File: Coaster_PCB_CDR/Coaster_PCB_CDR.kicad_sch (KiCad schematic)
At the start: 34 parts, among them J1 Vin, J10 GPIO_0-1, J11 5v, J12 5v, J13 GPIO_14-15, J14 5v, J15 GPIO_27-28, J16 5v, J17 5v, J2 Vin, J3 HC-05, J4 HC-05, J5 VCC_Batt, J6 3v3, J7 10V, J8 qwiic, J9 3v3, SW1 Vin_Switch, SW2 Vin_Switch, SW3 Vin_Switch, U1 PicoW, U2 LM2937xT

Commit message: final please
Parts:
- removed H2: M, MountingHole:MountingHole_4.3mm_M4_Pad_Via, symbol Mechanical:MountingHole_Pad
- added J10: qwiic, Connector_JST:JST_SH_SM04B-SRSS-TB_1x04-1MP_P1.00mm_Horizontal, symbol Connector_Generic:Conn_01x04
- renumbered H3 to H2, J10 to J12, J12 to J13, J13 to J15, J15 to J17, J17 to J18, J5 to J3, J3 to J4, J7 to J5, J4 to J6, J6 to J7, J9 to J8, J8 to J9
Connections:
- net +3V3: now also J10.2 (Pin_2)
- net GND: now also J10.1 (Pin_1)
- net GPIO0: now also J10.3 (Pin_3)
- net GPIO1: now also J10.4 (Pin_4)
- no-connect marks 13 -> 12
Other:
- moved on the sheet: C1, C2, D1, D2, H2, R1, SW1

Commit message: final finalish
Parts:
- added C1: 2200uF, Capacitor_THT:CP_Radial_D10.0mm_P5.00mm, symbol M5_BuggyProject-rescue:CP-Device
- SW1: value Vin_Switch -> sigma
- SW2: renamed from SW3; value Vin_Switch -> alpha
- SW3: renamed from SW2; value Vin_Switch -> beta
- renumbered C1 to C2, C2 to C3, J11 to J10, J12 to J11, J13 to J12, J14 to J13, J15 to J14, J16 to J15, J17 to J16, J10 to J17
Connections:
- net GND: now also C1.2
- net VCC_Batt: now also C1.1
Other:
- moved on the sheet: SW3

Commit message: some refinements
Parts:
- added J12: 5v, Connector_PinSocket_2.54mm:PinSocket_1x02_P2.54mm_Vertical, symbol Connector_Generic:Conn_01x02
- renumbered J12 to J13, J13 to J14, J14 to J15, J15 to J16, J16 to J17, J17 to J18, J18 to J19
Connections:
- net +5V: now also J12.2 (Pin_2)
- net GND: now also J12.1 (Pin_1)

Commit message: antooonie
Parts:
- removed J3: VCC_Batt, TestPoint:TestPoint_Plated_Hole_D5.0mm, symbol Connector_Generic:Conn_01x01
- J5: footprint TestPoint:TestPoint_Plated_Hole_D5.0mm -> TestPoint:TestPoint_Plated_Hole_D3.0mm
- R1: value 330 -> 1k; footprint Resistor_THT:R_Axial_DIN0204_L3.6mm_D1.6mm_P7.62mm_Horizontal -> Resistor_THT:R_Axial_DIN0207_L6.3mm_D2.5mm_P10.16mm_Horizontal
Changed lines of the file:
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@@
-    )
-  )
-  (global_label "VCC_Batt" (shape input) (at 101.6 130.81 90) (fields_autoplaced)
-    (effects (font (size 1.27 1.27)) (justify left))
-    (property "Intersheet References" "${INTERSHEET_REFS}" (id 0) (at 101.5206 119.9302 90)
-      (effects (font (size 1.27 1.27)) (justify left) hide)
     )
   )
@@
     (in_bom yes) (on_board yes)
     (property "Reference" "R1" (id 0) (at 97.79 35.7886 90))
-    (property "Value" "330" (id 1) (at 97.79 38.1 90)
+    (property "Value" "1k" (id 1) (at 97.79 38.1 90)
       (effects (font (size 1.016 1.016)))
     )
-    (property "Footprint" "Resistor_THT:R_Axial_DIN0204_L3.6mm_D1.6mm_P7.62mm_Horizontal" (id 2) (at 97.79 38.862 90)
+    (property "Footprint" "Resistor_THT:R_Axial_DIN0207_L6.3mm_D2.5mm_P10.16mm_Horizontal" (id 2) (at 97.79 38.862 90)
       (effects (font (size 1.27 1.27)) hide)
     )
@@
       (effects (font (size 1.27 1.27)) (justify left))
     )
-    (property "Footprint" "TestPoint:TestPoint_Plated_Hole_D5.0mm" (id 2) (at 109.22 135.89 0)
+    (property "Footprint" "TestPoint:TestPoint_Plated_Hole_D3.0mm" (id 2) (at 109.22 135.89 0)
       (effects (font (size 1.27 1.27)) hide)
     )
@@
     )
     (property "Datasheet" "" (id 3) (at 160.02 129.54 0)
-      (effects (font (size 1.27 1.27)) hide)
-    )
-    (pin "1")
-  )
-  (symbol (lib_id "Connector_Generic:Conn_01x01") (at 101.6 135.89 270) (unit 1)
-    (in_bom yes) (on_board yes)
-    (property "Reference" "J3" (id 0) (at 103.632 132.6388 90)
-      (effects (font (size 1.27 1.27)) (justify left))
-    )
-    (property "Value" "VCC_Batt" (id 1) (at 97.79 138.43 90)
-      (effects (font (size 1.27 1.27)) (justify left))
-    )
-    (property "Footprint" "TestPoint:TestPoint_Plated_Hole_D5.0mm" (id 2) (at 101.6 135.89 0)
-      (effects (font (size 1.27 1.27)) hide)
-    )
-    (property "Datasheet" "~" (id 3) (at 101.6 135.89 0)
       (effects (font (size 1.27 1.27)) hide)
     )
@@
       (reference "J2") (unit 1) (value "Vin") (footprint "Connector_PinSocket_2.54mm:PinSocket_1x02_P2.54mm_Vertical")
     )
-    (path "/406bc657-f0d9-4cdc-a558-cd9bffd22dd4"
-      (reference "J3") (unit 1) (value "VCC_Batt") (footprint "TestPoint:TestPoint_Plated_Hole_D5.0mm")
-    )
     (path "/ac0cdac4-5ad6-4885-bc81-46c93e1ce041"
       (reference "J4") (unit 1) (value "HC-05") (footprint "Connector_PinSocket_2.54mm:PinSocket_1x06_P2.54mm_Vertical")
     )
     (path "/00000000-0000-0000-0000-0000627eac87"
-      (reference "J5") (unit 1) (value "10V") (footprint "TestPoint:TestPoint_Plated_Hole_D5.0mm")
+      (reference "J5") (unit 1) (value "10V") (footprint "TestPoint:TestPoint_Plated_Hole_D3.0mm")
     )
     (path "/7bcc4302-a9ff-46a0-92cd-33fd1db4d7ac"
@@
     )
     (path "/00000000-0000-0000-0000-000061de06ec"
-      (reference "R1") (unit 1) (value "330") (footprint "Resistor_THT:R_Axial_DIN0204_L3.6mm_D1.6mm_P7.62mm_Horizontal")
+      (reference "R1") (unit 1) (value "1k") (footprint "Resistor_THT:R_Axial_DIN0207_L6.3mm_D2.5mm_P10.16mm_Horizontal")
     )
     (path "/00000000-0000-0000-0000-000061d314d6"

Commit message: done with fdr pcb?
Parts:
- removed C1: 2200uF, Capacitor_THT:CP_Radial_D10.0mm_P5.00mm, symbol M5_BuggyProject-rescue:CP-Device
- removed J10, J12, J14, J16, J19: 5v, Connector_PinSocket_2.54mm:PinSocket_1x02_P2.54mm_Vertical, symbol Connector_Generic:Conn_01x02
- removed J2: Vin, Connector_PinSocket_2.54mm:PinSocket_1x02_P2.54mm_Vertical, symbol Connector_Generic:Conn_01x02
- removed J6: HC-05, Connector_PinSocket_2.54mm:PinSocket_1x06_P2.54mm_Vertical, symbol Connector_Generic:Conn_01x06
- removed J7: 3v3, Connector_PinSocket_2.54mm:PinSocket_1x02_P2.54mm_Vertical, symbol Connector_Generic:Conn_01x02
- removed SW2: alpha, Buggy_Footprints:omar_3pin_switch, symbol Switch:SW_SPDT
- removed SW3: beta, Buggy_Footprints:omar_3pin_switch, symbol Switch:SW_SPDT
- added SW1: sigma, Buggy_Footprints:omar_3pin_switch, symbol Switch:SW_SPDT
- renumbered C2 to C1, C3 to C2, J18 to J10, J4 to J2, J5 to J3, J8 to J4, J9 to J5, J11 to J6, J13 to J7, J15 to J8, J17 to J9, SW1 to SW2
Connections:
- net GPIO0: now also J2.5 (Pin_5); no longer J10.3 (Pin_3), J5.3 (Pin_3)
- net GPIO1: now also J2.4 (Pin_4); no longer J10.4 (Pin_4), J5.4 (Pin_4)
- net VCC: now also SW1.1 (A), SW1.2 (B), SW1.3 (C)
- net GPIO16: no longer names the net of U1.21 (GPIO16)
- net GPIO16: no longer J2.4 (Pin_4)
- net GPIO17: no longer names the net of U1.22 (GPIO17)
- net GPIO17: no longer J2.5 (Pin_5)
- net GPIO4 renamed SDA
- net SDA: now also J10.3 (Pin_3), J5.3 (Pin_3)
- net GPIO5 renamed SCL
- net SCL: now also J10.4 (Pin_4), J5.4 (Pin_4)

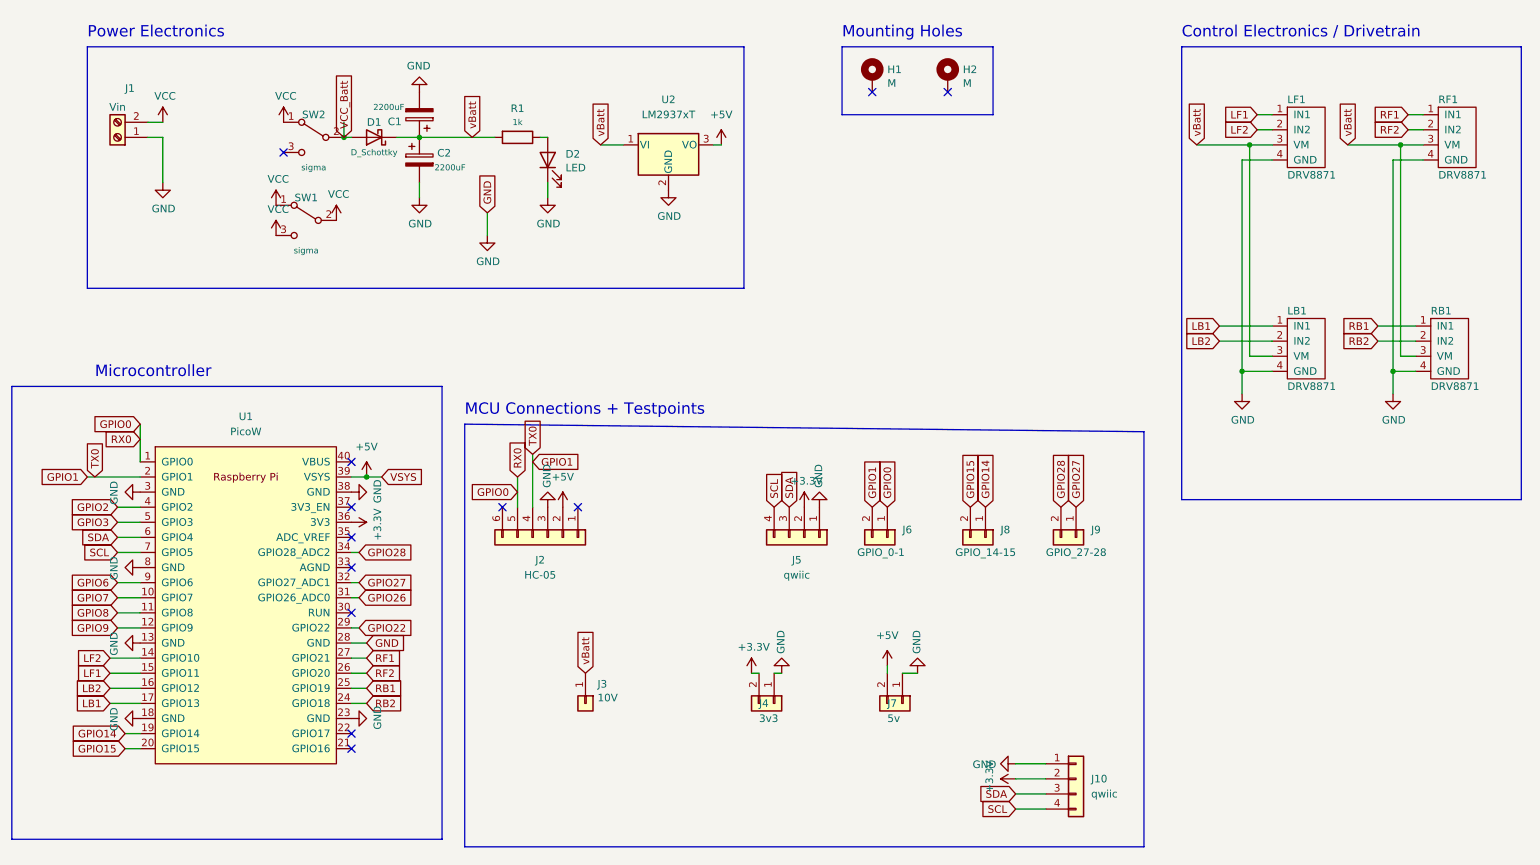
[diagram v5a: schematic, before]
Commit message: fdr pcb minimized
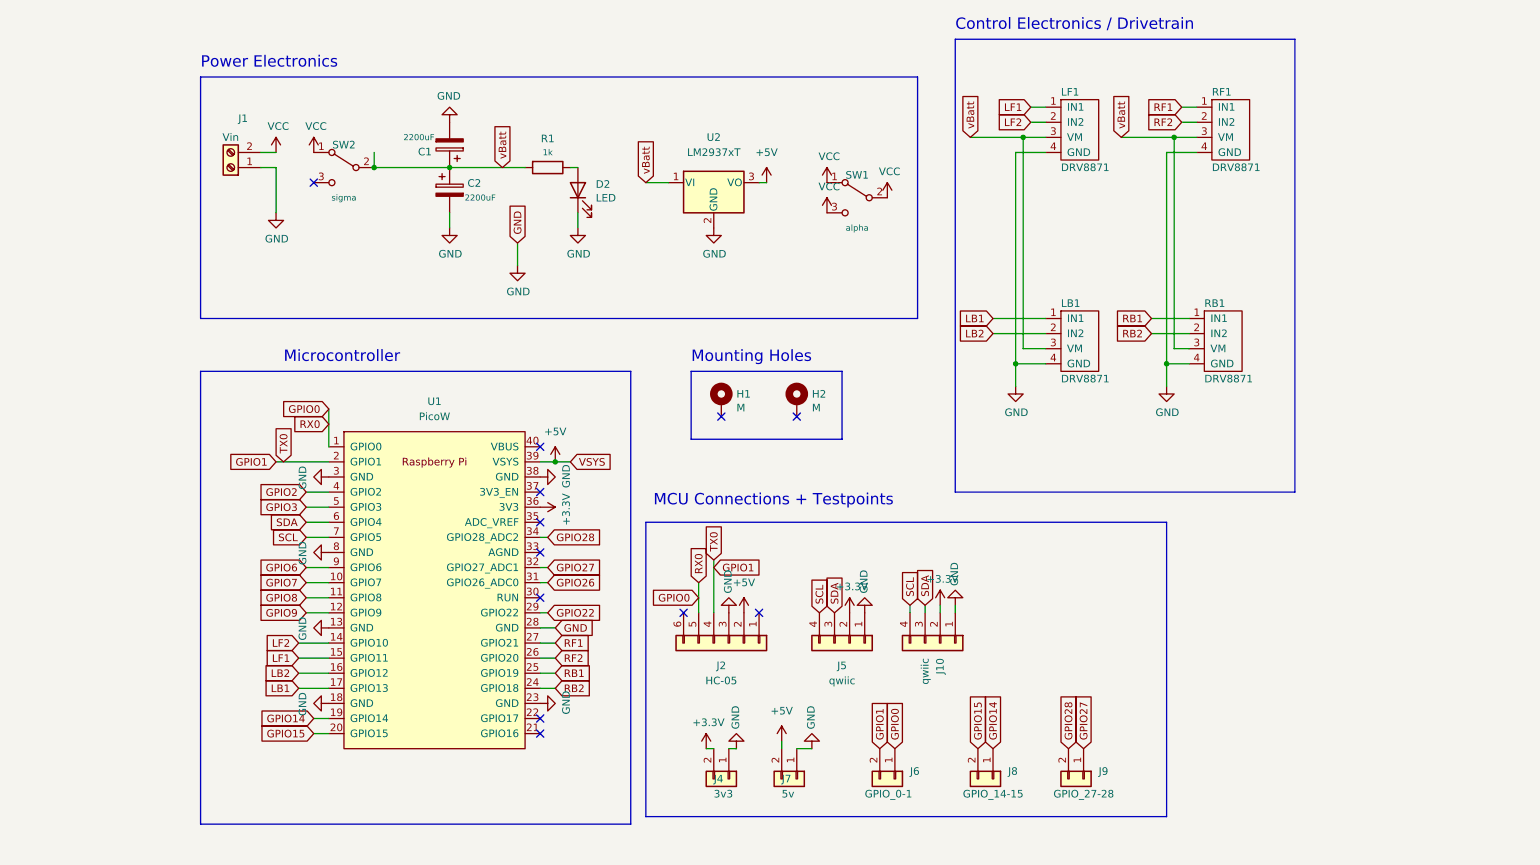
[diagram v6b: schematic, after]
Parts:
- removed D1: D_Schottky, Package_TO_SOT_THT:TO-220-2_Vertical, symbol Device:D_Schottky
- removed J3: 10V, TestPoint:TestPoint_Plated_Hole_D3.0mm, symbol Connector_Generic:Conn_01x01
- SW1: value sigma -> alpha
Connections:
- net VCC_Batt is gone; now on net vBatt: SW2.2 (B)
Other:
- moved on the sheet: C1, C2, D2, H1, H2, J1, J10, J2, J4, J5, J6, J7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

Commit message: changed LDO foot print
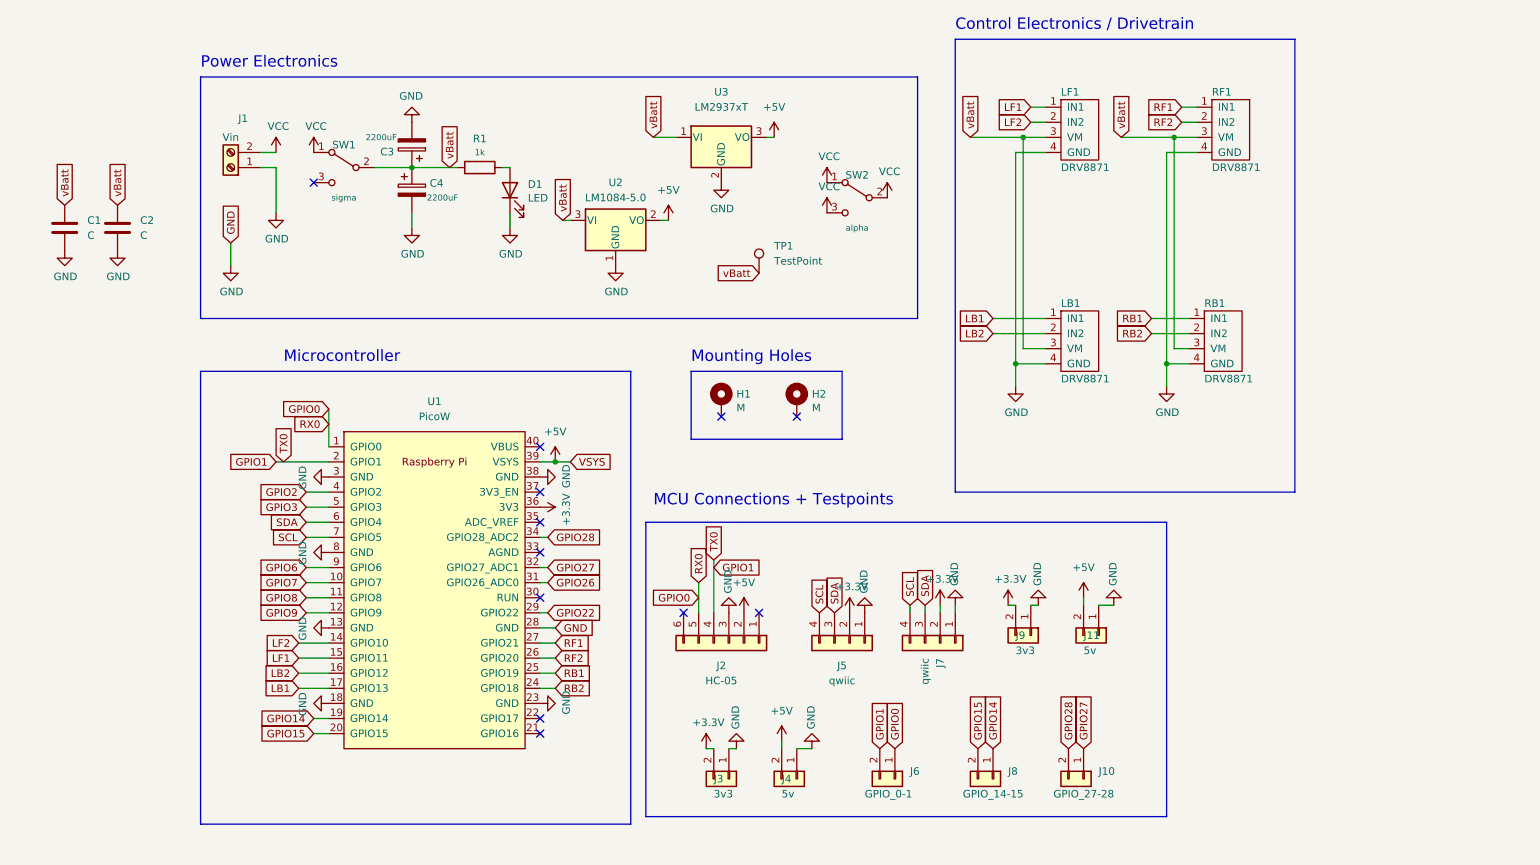
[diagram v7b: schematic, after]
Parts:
- added C1, C2: C, Capacitor_THT:C_Disc_D3.0mm_W1.6mm_P2.50mm, symbol Device:C
- added J11: 5v, Connector_PinSocket_2.54mm:PinSocket_1x02_P2.54mm_Vertical, symbol Connector_Generic:Conn_01x02
- added J9: 3v3, Connector_PinSocket_2.54mm:PinSocket_1x02_P2.54mm_Vertical, symbol Connector_Generic:Conn_01x02
- added TP1: TestPoint, TestPoint:TestPoint_THTPad_D1.5mm_Drill0.7mm, symbol Connector:TestPoint
- added U2: LM1084-5.0, Package_TO_SOT_THT:TO-220-3_Vertical, symbol Regulator_Linear:LM1084-5.0
- renumbered C1 to C3, C2 to C4, D2 to D1, J9 to J10, J4 to J3, J7 to J4, J10 to J7, SW2 to SW1, SW1 to SW2, U2 to U3
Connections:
- net +3V3: now also J9.2 (Pin_2)
- net +5V: now also J11.2 (Pin_2), U2.2 (VO)
- net GND: now also C1.2, C2.2, J11.1 (Pin_1), J9.1 (Pin_1), U2.1 (GND)
- net vBatt: now also C1.1, C2.1, TP1.1, U2.3 (VI)
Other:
- moved on the sheet: C3, C4, D1, R1, U3
